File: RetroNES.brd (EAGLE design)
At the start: 50.8 x 37.3 mm, 8 parts, among them IC1 ATMEGA32U4-AU

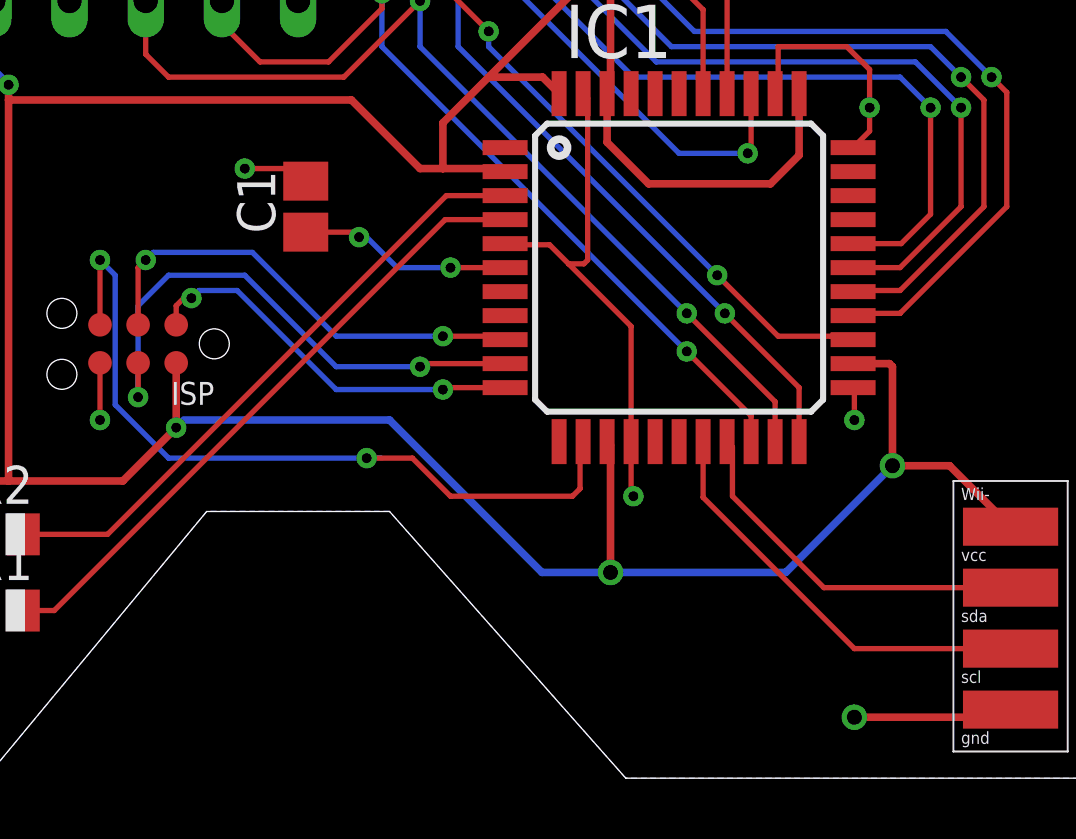
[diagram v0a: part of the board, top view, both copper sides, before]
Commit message: Added the source code.
The source code is essentially the same as the retropad project and
massaged to make it work with hard wired buttons.
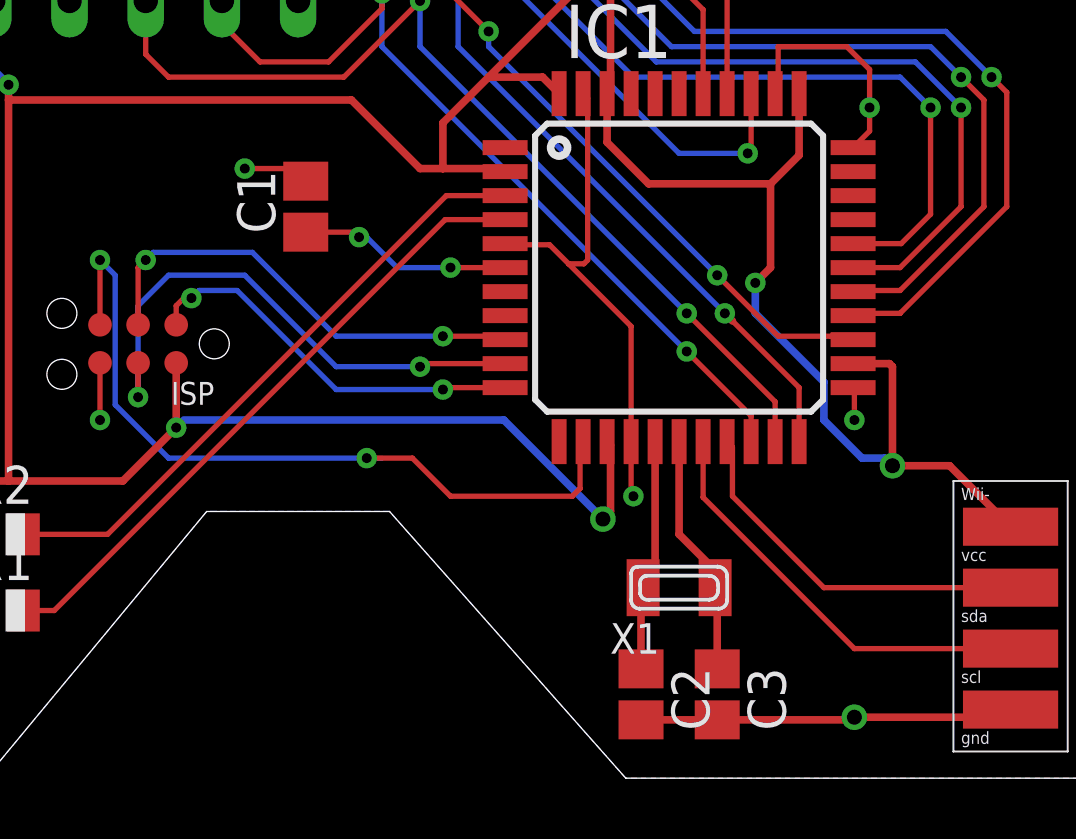
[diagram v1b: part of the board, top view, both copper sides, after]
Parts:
- added C2: 16pf, adafruit:C0805
- added C3: 16pF, adafruit:C0805
- added X1: (no value), adafruit:XTAL3215
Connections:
- new net XTAL1: C3.1, IC1.17, X1.P$1
- new net XTAL2: C2.1, IC1.16, X1.P$2
- net GND: now also C2.2, C3.2
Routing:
- net XTAL1: track 0.00 -> 8.10 mm
- net XTAL2: track 0.00 -> 7.77 mm
- net GND: track 39.0 -> 46.1 mm
- net VCC: track 130.6 -> 129.0 mm, vias 4 -> 5
